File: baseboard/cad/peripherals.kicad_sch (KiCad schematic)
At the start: 32 parts, among them J12 6-440054-2, J13 6-440054-2, J14 6-440129-2, J15 6-440129-2, J17 6-440054-2, J18 6-440054-2, J19 6-440129-2, J20 6-440129-2, Q1 Q_Dual_NMOS_S1G1D2S2G2D1, SW1 FOOTSWITCH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

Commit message: more schematic cleanup
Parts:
- U2: footprint (none) -> Package_TO_SOT_SMD:SOT-363_SC-70-6
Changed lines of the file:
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@@
       (effects (font (size 1.27 1.27)))
     )
-    (property "Footprint" "" (at 77.47 76.2 0)
+    (property "Footprint" "Package_TO_SOT_SMD:SOT-363_SC-70-6" (at 77.47 76.2 0)
       (effects (font (size 1.27 1.27)) hide)
     )
@@
       (effects (font (size 1.27 1.27)) (justify left))
     )
-    (property "Footprint" "" (at 127 44.45 0)
+    (property "Footprint" "Package_TO_SOT_SMD:SOT-363_SC-70-6" (at 127 44.45 0)
       (effects (font (size 1.27 1.27)) hide)
     )
@@
       (effects (font (size 1.27 1.27)))
     )
-    (property "Footprint" "" (at 203.2 76.2 0)
-      (effects (font (size 1.27 1.27)) hide)
-    )
+    (property "Footprint" "Package_TO_SOT_SMD:SOT-363_SC-70-6" (at 203.2 76.2 0)
+      (effects (font (size 1.27 1.27)) hide)
+    )

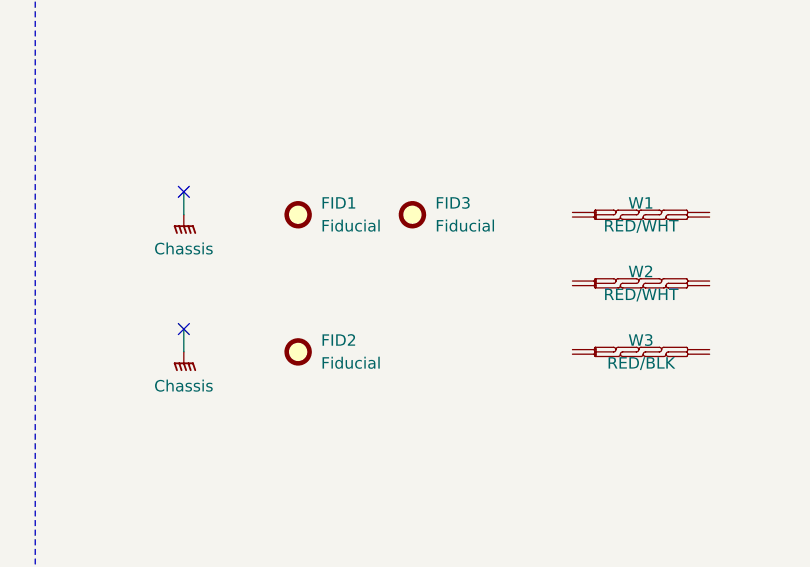
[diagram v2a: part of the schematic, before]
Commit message: drawing sheet updates and general prep for fab
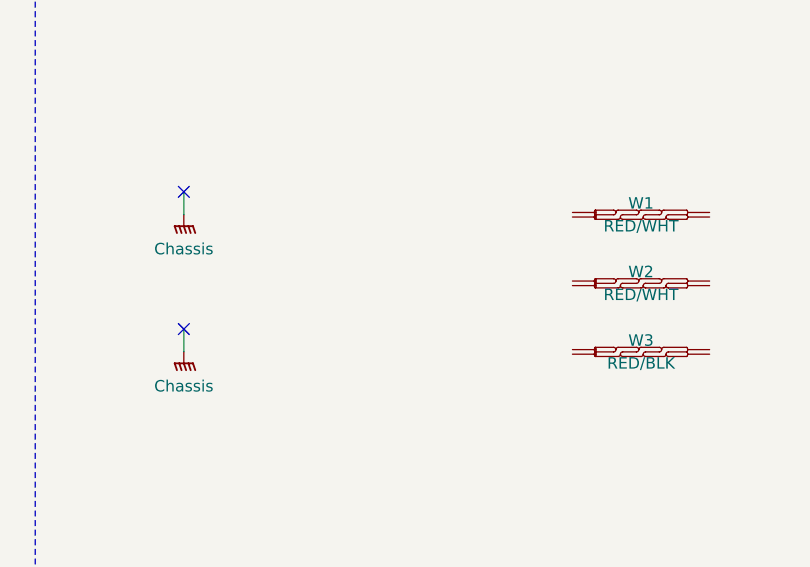
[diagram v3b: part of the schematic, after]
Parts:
- removed FID1, FID2, FID3: Fiducial, Fiducial:Fiducial_0.5mm_Mask1mm, symbol Mechanical:Fiducial
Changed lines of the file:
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@@
-    )
-  )
-  (symbol (lib_id "Mechanical:Fiducial") (at 168.91 151.13 0) (unit 1)
-    (in_bom yes) (on_board yes) (dnp no) (fields_autoplaced)
-    (property "Reference" "FID2" (at 171.45 149.8599 0)
-      (effects (font (size 1.27 1.27)) (justify left))
-    )
-    (property "Value" "Fiducial" (at 171.45 152.3999 0)
-      (effects (font (size 1.27 1.27)) (justify left))
-    )
-    (property "Footprint" "Fiducial:Fiducial_0.5mm_Mask1mm" (at 168.91 151.13 0)
-      (effects (font (size 1.27 1.27)) hide)
-    )
-    (property "Datasheet" "~" (at 168.91 151.13 0)
-      (effects (font (size 1.27 1.27)) hide)
-    )
-    (property "Manufacturer" "N/A" (at 168.91 151.13 0)
-      (effects (font (size 1.27 1.27)) hide)
-    )
-    (instances
-      (project "1590N1 IO Board"
-        (path "/190888c1-6ce2-4681-a836-dc477e444e49/e436358c-d730-4540-92b5-b7475a7c4a63"
-          (reference "FID2") (unit 1)
-        )
-        (path "/190888c1-6ce2-4681-a836-dc477e444e49/2e4f7641-7de0-4dea-9f64-f5ec09624375"
-          (reference "FID2") (unit 1)
-        )
-        (path "/190888c1-6ce2-4681-a836-dc477e444e49"
-          (reference "FID?") (unit 1)
-        )
-        (path "/190888c1-6ce2-4681-a836-dc477e444e49/a050f331-207a-415a-9776-ea47c7d16f9f"
-          (reference "FID2") (unit 1)
-        )
-      )
     )
   )
@@
         (path "/190888c1-6ce2-4681-a836-dc477e444e49/a050f331-207a-415a-9776-ea47c7d16f9f"
           (reference "#PWR033") (unit 1)
-        )
-      )
-    )
-  )
-  (symbol (lib_id "Mechanical:Fiducial") (at 181.61 135.89 0) (unit 1)
-    (in_bom yes) (on_board yes) (dnp no) (fields_autoplaced)
-    (property "Reference" "FID3" (at 184.15 134.6199 0)
-      (effects (font (size 1.27 1.27)) (justify left))
-    )
-    (property "Value" "Fiducial" (at 184.15 137.1599 0)
-      (effects (font (size 1.27 1.27)) (justify left))
-    )
-    (property "Footprint" "Fiducial:Fiducial_0.5mm_Mask1mm" (at 181.61 135.89 0)
-      (effects (font (size 1.27 1.27)) hide)
-    )
-    (property "Datasheet" "~" (at 181.61 135.89 0)
-      (effects (font (size 1.27 1.27)) hide)
-    )
-    (property "Manufacturer" "N/A" (at 181.61 135.89 0)
-      (effects (font (size 1.27 1.27)) hide)
-    )
-    (instances
-      (project "1590N1 IO Board"
-        (path "/190888c1-6ce2-4681-a836-dc477e444e49/e436358c-d730-4540-92b5-b7475a7c4a63"
-          (reference "FID3") (unit 1)
-        )
-        (path "/190888c1-6ce2-4681-a836-dc477e444e49/2e4f7641-7de0-4dea-9f64-f5ec09624375"
-          (reference "FID3") (unit 1)
-        )
-        (path "/190888c1-6ce2-4681-a836-dc477e444e49"
-          (reference "FID?") (unit 1)
-        )
-        (path "/190888c1-6ce2-4681-a836-dc477e444e49/a050f331-207a-415a-9776-ea47c7d16f9f"
-          (reference "FID3") (unit 1)
         )
       )
@@
         )
       )
-    )
-  )
-  (symbol (lib_id "Mechanical:Fiducial") (at 168.91 135.89 0) (unit 1)
-    (in_bom yes) (on_board yes) (dnp no) (fields_autoplaced)
-    (property "Reference" "FID1" (at 171.45 134.6199 0)
-      (effects (font (size 1.27 1.27)) (justify left))
-    )
-    (property "Value" "Fiducial" (at 171.45 137.1599 0)
-      (effects (font (size 1.27 1.27)) (justify left))
-    )
-    (property "Footprint" "Fiducial:Fiducial_0.5mm_Mask1mm" (at 168.91 135.89 0)
-      (effects (font (size 1.27 1.27)) hide)
-    )
-    (property "Datasheet" "~" (at 168.91 135.89 0)
-      (effects (font (size 1.27 1.27)) hide)
-    )
-    (property "Manufacturer" "N/A" (at 168.91 135.89 0)
-      (effects (font (size 1.27 1.27)) hide)
-    )
-    (instances
-      (project "1590N1 IO Board"
-        (path "/190888c1-6ce2-4681-a836-dc477e444e49/e436358c-d730-4540-92b5-b7475a7c4a63"
-          (reference "FID1") (unit 1)
-        )
-        (path "/190888c1-6ce2-4681-a836-dc477e444e49/2e4f7641-7de0-4dea-9f64-f5ec09624375"
-          (reference "FID1") (unit 1)
-        )
-        (path "/190888c1-6ce2-4681-a836-dc477e444e49"
-          (reference "FID?") (unit 1)
-        )
-        (path "/190888c1-6ce2-4681-a836-dc477e444e49/a050f331-207a-415a-9776-ea47c7d16f9f"
-          (reference "FID1") (unit 1)
-        )
-      )

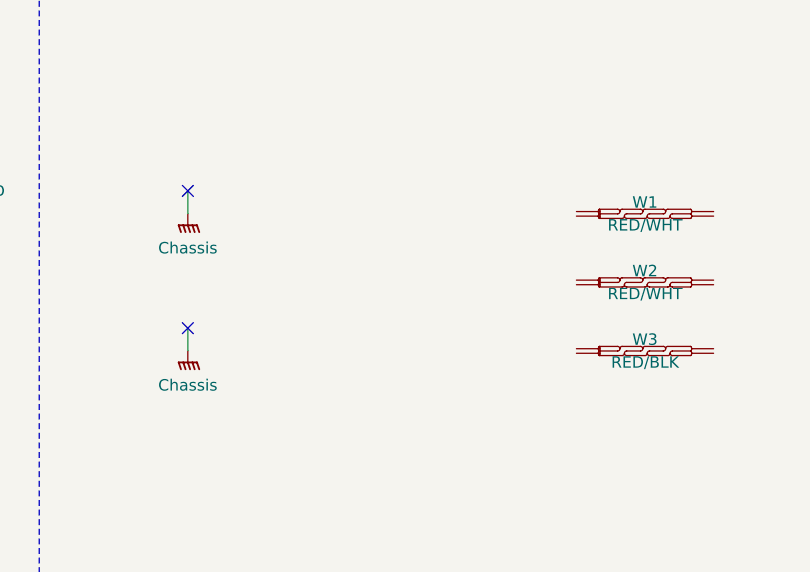
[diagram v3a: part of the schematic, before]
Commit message: cleaning up layout, added graphic symbols
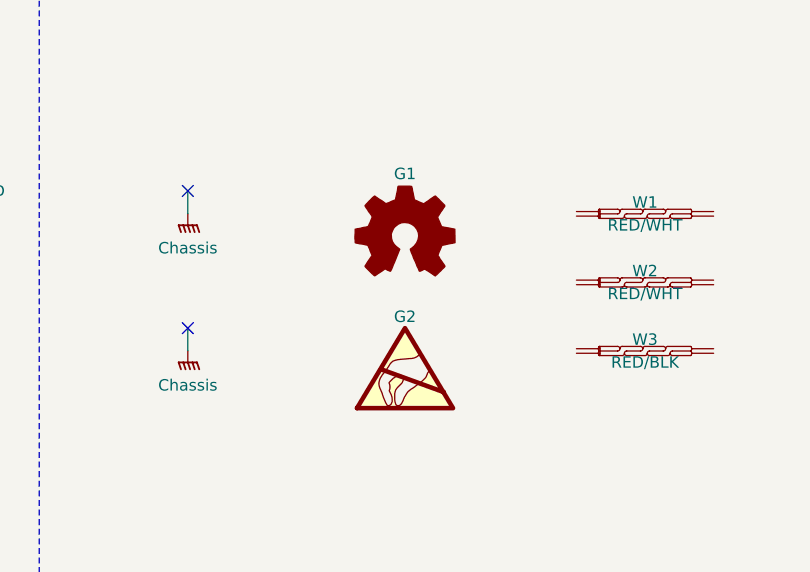
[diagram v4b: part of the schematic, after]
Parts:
- added G1: Logo_Open_Hardware_Small, Symbol:OSHW-Logo_7.5x8mm_SilkScreen, symbol Graphic:Logo_Open_Hardware_Small
- added G2: SYM_ESD_Small, Symbol:ESD-Logo_8.9x8mm_SilkScreen, symbol Graphic:SYM_ESD_Large
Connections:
- net GNDPWR renamed PWR
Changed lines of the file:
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@@
+    )
+  )
+  (symbol (lib_id "Graphic:SYM_ESD_Large") (at 180.34 152.4 0) (unit 1)
+    (in_bom no) (on_board yes) (dnp no)
+    (property "Reference" "G2" (at 180.34 147.32 0)
+      (effects (font (size 1.27 1.27)))
+    )
+    (property "Value" "SYM_ESD_Small" (at 180.34 155.575 0)
+      (effects (font (size 1.27 1.27)) hide)
+    )
+    (property "Footprint" "Symbol:ESD-Logo_8.9x8mm_SilkScreen" (at 180.213 153.162 0)
+      (effects (font (size 1.27 1.27)) hide)
+    )
+    (property "Datasheet" "~" (at 180.213 153.162 0)
+      (effects (font (size 1.27 1.27)) hide)
+    )
+    (property "Sim.Enable" "0" (at 180.34 152.4 0)
+      (effects (font (size 1.27 1.27)) hide)
+    )
+    (instances
+      (project "1590N1 IO Board"
+        (path "/190888c1-6ce2-4681-a836-dc477e444e49/a050f331-207a-415a-9776-ea47c7d16f9f"
+          (reference "G2") (unit 1)
+        )
+      )
     )
   )
@@
         )
         (path "/190888c1-6ce2-4681-a836-dc477e444e49/a050f331-207a-415a-9776-ea47c7d16f9f"
-          (reference "G2") (unit 1)
+          (reference "CHS2") (unit 1)
         )
       )
@@
         (path "/190888c1-6ce2-4681-a836-dc477e444e49/a050f331-207a-415a-9776-ea47c7d16f9f"
           (reference "#PWR048") (unit 1)
+        )
+      )
+    )
+  )
+  (symbol (lib_id "Graphic:Logo_Open_Hardware_Small") (at 180.34 138.43 0) (unit 1)
+    (in_bom no) (on_board yes) (dnp no) (fields_autoplaced)
+    (property "Reference" "G1" (at 180.34 131.445 0)
+      (effects (font (size 1.27 1.27)))
+    )
+    (property "Value" "Logo_Open_Hardware_Small" (at 180.34 144.145 0)
+      (effects (font (size 1.27 1.27)) hide)
+    )
+    (property "Footprint" "Symbol:OSHW-Logo_7.5x8mm_SilkScreen" (at 180.34 138.43 0)
+      (effects (font (size 1.27 1.27)) hide)
+    )
+    (property "Datasheet" "~" (at 180.34 138.43 0)
+      (effects (font (size 1.27 1.27)) hide)
+    )
+    (property "Sim.Enable" "0" (at 180.34 138.43 0)
+      (effects (font (size 1.27 1.27)) hide)
+    )
+    (instances
+      (project "1590N1 IO Board"
+        (path "/190888c1-6ce2-4681-a836-dc477e444e49/a050f331-207a-415a-9776-ea47c7d16f9f"
+          (reference "G1") (unit 1)
         )
       )
@@
         )
         (path "/190888c1-6ce2-4681-a836-dc477e444e49/a050f331-207a-415a-9776-ea47c7d16f9f"
-          (reference "G3") (unit 1)
-        )
-      )
+          (reference "CHS3") (unit 1)
+        )
+      )
